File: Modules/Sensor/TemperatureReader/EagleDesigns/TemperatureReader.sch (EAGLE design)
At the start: 11 parts, among them U1 MLX90614, U2 ATMEGA328P_TQFP

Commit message: fixed eagle files for new modules
SIN/SOUT was not correctly connected in them.
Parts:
- C3: device adafruit:C-USC0402 -> adafruit:C-USC0603
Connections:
- removed net 1X3SIN-SOUT: JP1.1, JP1.4, R1.2
- net 1X3SIN: now also JP1.4, R1.2
- net 1X3SOUT: now also JP1.1
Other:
- moved on the sheet: C1, C2, C3, JP1, JP2, R1, R2, R4, U1, U2

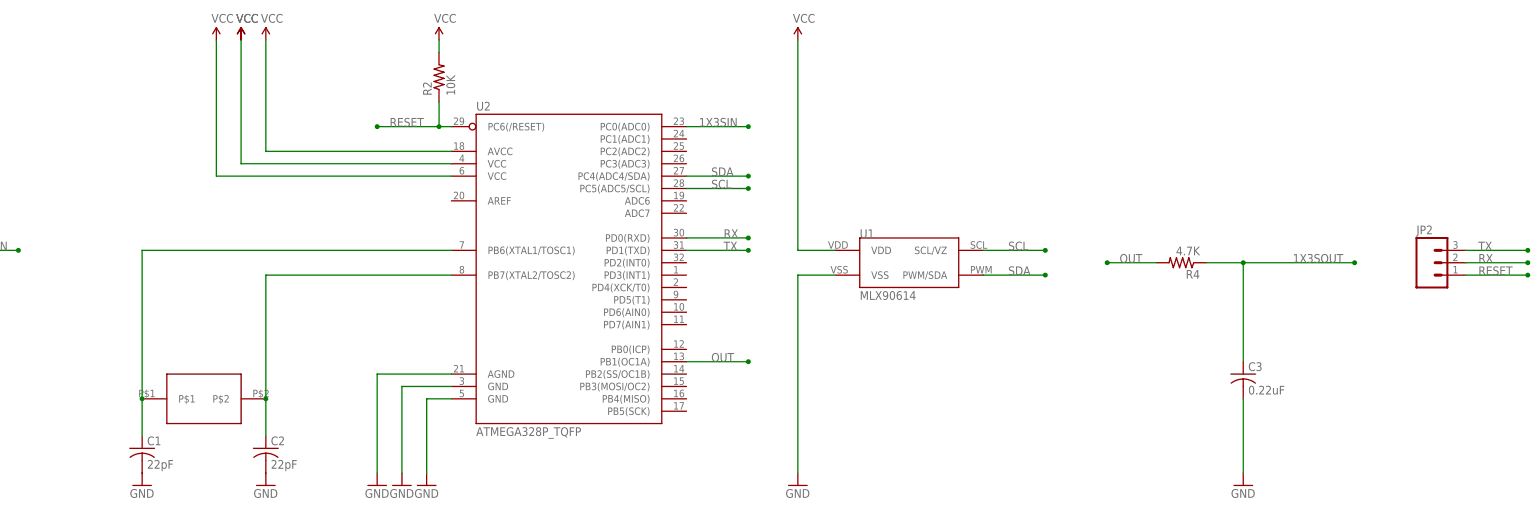
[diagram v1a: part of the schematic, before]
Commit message: TemperatureReader: removed crystal, modified to work with new bootloader #31
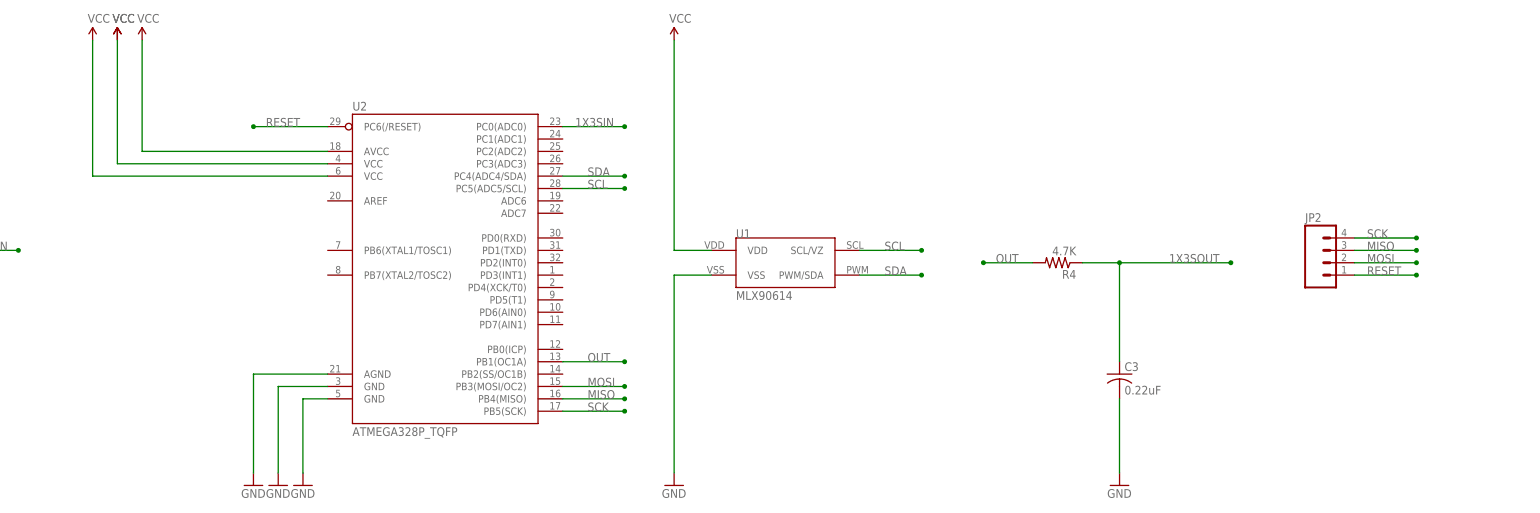
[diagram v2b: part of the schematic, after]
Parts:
- removed C1, C2: 22pF, adafruit:C-USC0603
- removed R2: 10K, resistor:R-US_R0603
- removed U$2: NX503, MakerWear:NX503
- JP2: device SparkFun-Connectors:M03PTH -> SparkFun-Connectors:M04PTH
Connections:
- removed net N$1: C1.1, U$2.P$1, U2.PB6(XTAL1/TOSC1)
- removed net N$3: C2.1, U$2.P$2, U2.PB7(XTAL2/TOSC2)
- removed net RX: JP2.2, U2.PD0(RXD)
- removed net TX: JP2.3, U2.PD1(TXD)
- new net MISO: JP2.3, U2.PB4(MISO)
- new net MOSI: JP2.2, U2.PB3(MOSI/OC2)
- new net SCK: JP2.4, U2.PB5(SCK)
- net GND: no longer C1.2, C2.2
- net RESET: no longer R2.1
- net VCC: no longer R2.2
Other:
- moved on the sheet: C3, R4, U1, U2
